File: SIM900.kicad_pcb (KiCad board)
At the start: 4 copper layers, 88 x 127 mm, 72 parts, among them J1 Conn_01x05, J11 Conn_Coaxial_Power, J12 AudioJack2_Ground, J13 AudioJack2_Ground, J2 Conn_01x04, J3 Conn_01x04, J4 Conn_01x06, J5 Conn_01x02, J6 Conn_01x06, J7 Conn_01x03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

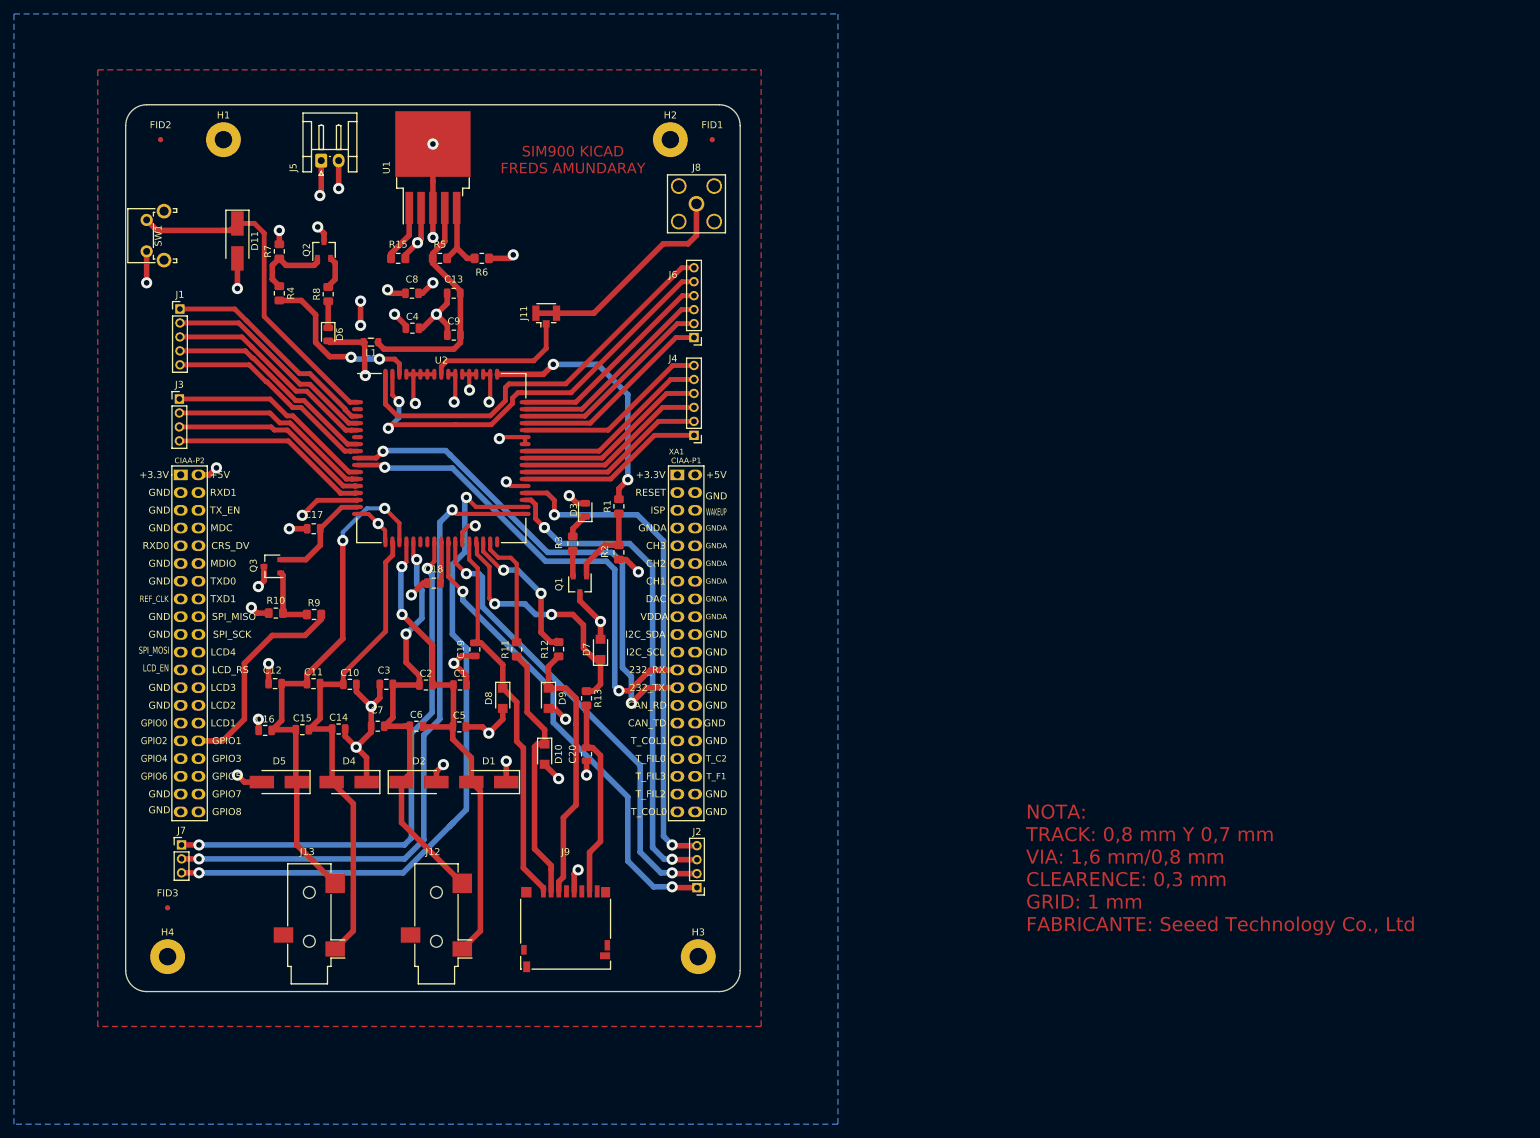
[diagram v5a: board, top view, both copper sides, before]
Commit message: Correccion de los comentarios realizados por el profesor al PCB
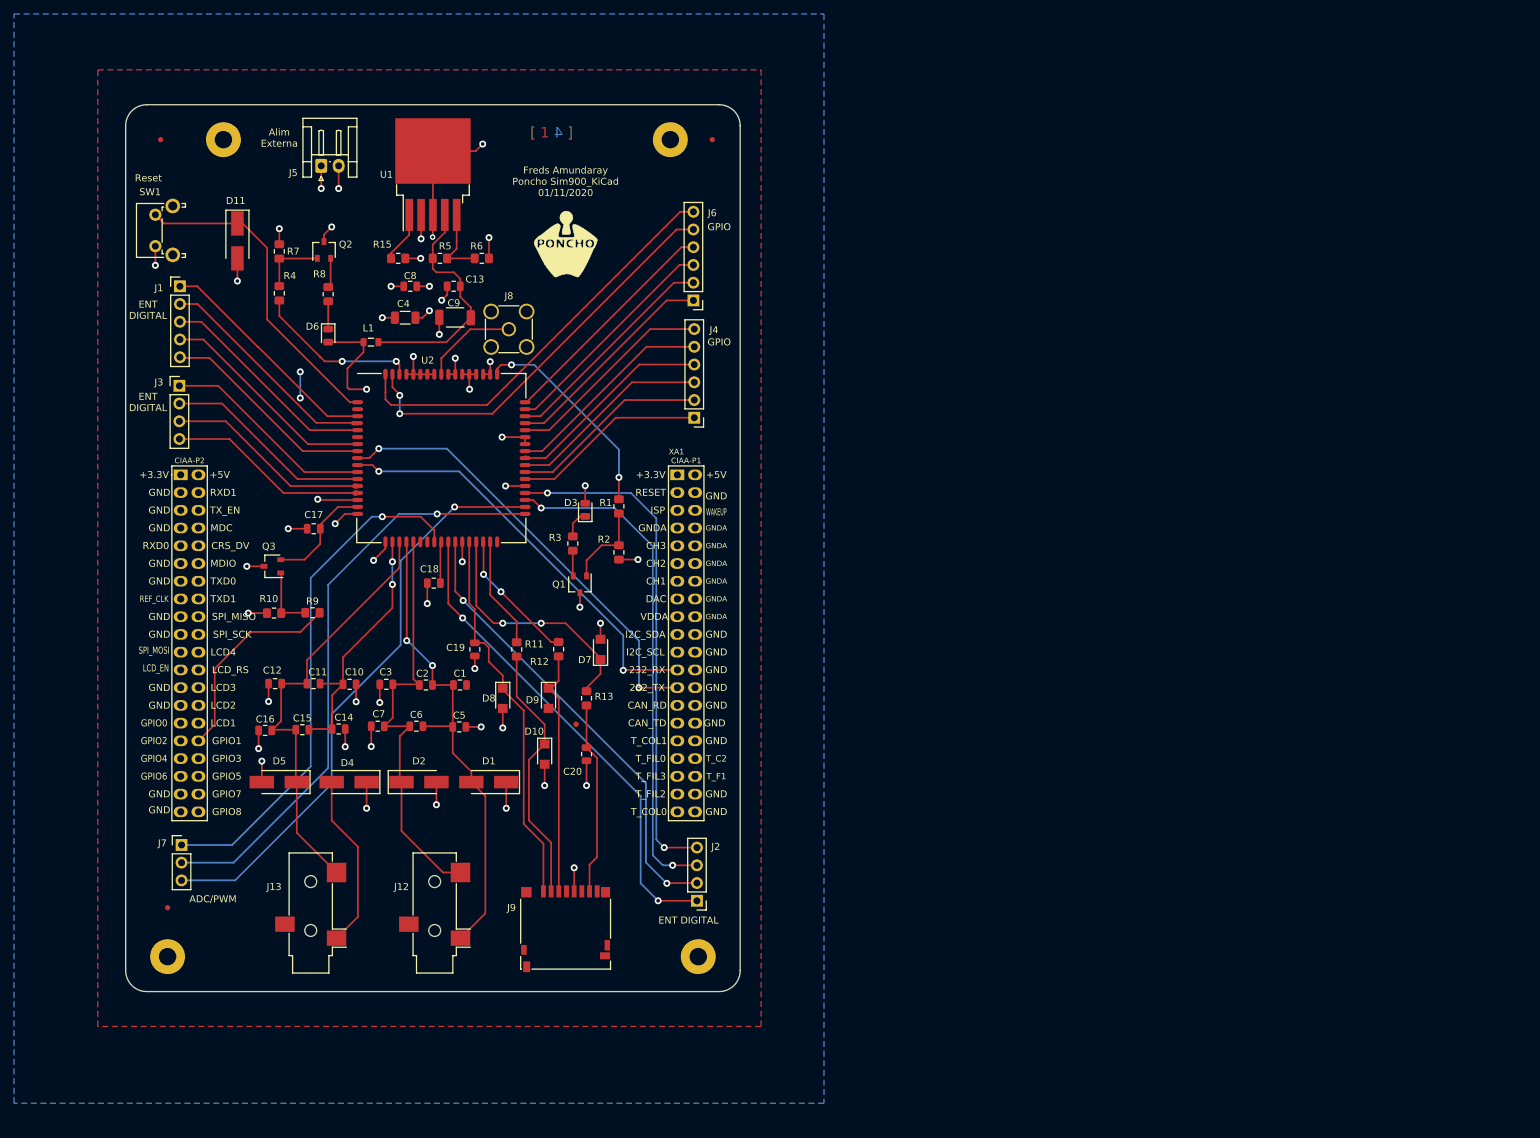
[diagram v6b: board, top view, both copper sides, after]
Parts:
- removed J11: Conn_Coaxial_Power, Connector_Coaxial:U.FL_Hirose_U.FL-R-SMT-1_Vertical
- added G***: LOGO, Poncho_Esqueleto:Logo_Poncho, F.Cu at (112.0, 58.0)
- C4: footprint Capacitor_SMD:C_0805_2012Metric -> Capacitor_SMD:C_1206_3216Metric
- C9: footprint Capacitor_SMD:C_0805_2012Metric -> Footprint:C_2312_2020Metric_Pad3.2x6.0mm_HandSolder
- J1: footprint Connector_PinHeader_2.00mm:PinHeader_1x05_P2.00mm_Vertical -> Connector_PinHeader_2.54mm:PinHeader_1x05_P2.54mm_Vertical
- J2, J3: footprint Connector_PinHeader_2.00mm:PinHeader_1x04_P2.00mm_Vertical -> Connector_PinHeader_2.54mm:PinHeader_1x04_P2.54mm_Vertical
- J4, J6: footprint Connector_PinHeader_2.00mm:PinHeader_1x06_P2.00mm_Vertical -> Connector_PinHeader_2.54mm:PinHeader_1x06_P2.54mm_Vertical
- J7: footprint Connector_PinHeader_2.00mm:PinHeader_1x03_P2.00mm_Vertical -> Connector_PinHeader_2.54mm:PinHeader_1x03_P2.54mm_Vertical
- J8: footprint Connector_Coaxial:SMA_Amphenol_132203-12_Horizontal -> Connector_Coaxial:SMA_Amphenol_901-144_Vertical
- moved J8 32.3 mm to (103.9, 70.2), turned to 0 degrees
- moved J6 5.32 mm to (130.3, 66.0)
- moved J1 3.25 mm to (56.8, 64.0)
- moved J4 2.52 mm to (130.4, 82.8)
- moved C9 2.50 mm to (96.1, 68.5)
- moved J3 1.89 mm to (56.7, 78.2)
- moved J2 1.89 mm to (130.8, 152.0)
- moved C4 1.82 mm to (89.0, 68.5), turned to 180 degrees
- moved J12 1.57 mm to (93.2, 153.8)
- moved J13 1.56 mm to (75.5, 153.8)
- moved SW1 1.46 mm to (53.2, 58.2)
- moved C8 1.03 mm to (89.8, 64.0)
- moved C13 1.00 mm to (96.0, 64.0)
- moved U1 1.00 mm to (93.0, 48.0)
- moved J5 0.75 mm to (77.0, 46.8)
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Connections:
- J8 pad 1: Net-(J11-Pad2) -> Net-(J8-Pad1)
- U2 pad 60: Net-(J11-Pad1) -> Net-(J8-Pad1)
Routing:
- net GND: track 173.2 -> 140.6 mm, vias 36 -> 43
- net Net-(J11-Pad2): track 32.1 -> 0.00 mm
- net Net-(J11-Pad1): track 20.7 -> 0.00 mm
- net Net-(J7-Pad3): track 100.8 -> 84.3 mm, vias 2 -> 1
- net Net-(J8-Pad1): track 0.00 -> 13.7 mm
- net Net-(C11-Pad1): track 76.3 -> 63.1 mm, vias 2 -> 0
- net +5V: track 77.5 -> 64.7 mm
- net Net-(J5-Pad1): track 67.4 -> 55.8 mm
- net Net-(J7-Pad2): track 95.4 -> 85.3 mm, vias 2 -> 1
- net /TXD: track 70.3 -> 60.9 mm
- net Net-(C10-Pad1): track 71.3 -> 62.5 mm, vias 0 -> 2
- net /RXD: track 73.0 -> 64.5 mm
- net /NETLIGHT: track 37.1 -> 31.1 mm
- net Net-(J7-Pad1): track 77.7 -> 73.9 mm, vias 2 -> 1
- net Net-(D9-Pad1): track 38.4 -> 35.1 mm
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- added copper zone on In2.Cu_VCD, net +3V3
- added copper zone on In1.Cu_GND, net GND
- removed copper zone on In1.Cu_VCD, net +3V3
- removed copper zone on In2.Cu_GND, net GND
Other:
- net class Default: clearance 0.3 -> 0.25
- rule trace_clearance: 0.3 -> 0.25
- board text added: "ADC/PWM"
- board text added: "Alim Externa"
- board text added: "ENT DIGITAL"
- board text added: "Freds Amundaray Poncho Sim900_KiCad 01/11/2020"
- board text added: "GPIO"
- board text added: "Nota: Minimos (MAYER 10 mils) Track: 0,25 mm Via: 1,0/ 0,5 mm Clearence: 0,25 mm distance to edge: 0,3 mm Grid: 1 mm / 0,5 mm / 0,25 mm Terminacion: HASL sin plomo"
- board text added: "Reset"
- board text added: "[ 1 ]"
- board text added: "[ 2 ]"
- board text added: "[ 3 ]"
- board text added: "[ 4 ]"
- board text removed: "NOTA: TRACK: 0,8 mm Y 0,7 mm VIA: 1,6 mm/0,8 mm CLEARENCE: 0,3 mm GRID: 1 mm FABRICANTE: Seeed Technology Co., Ltd"
- board text removed: "SIM900 KICAD FREDS AMUNDARAY"

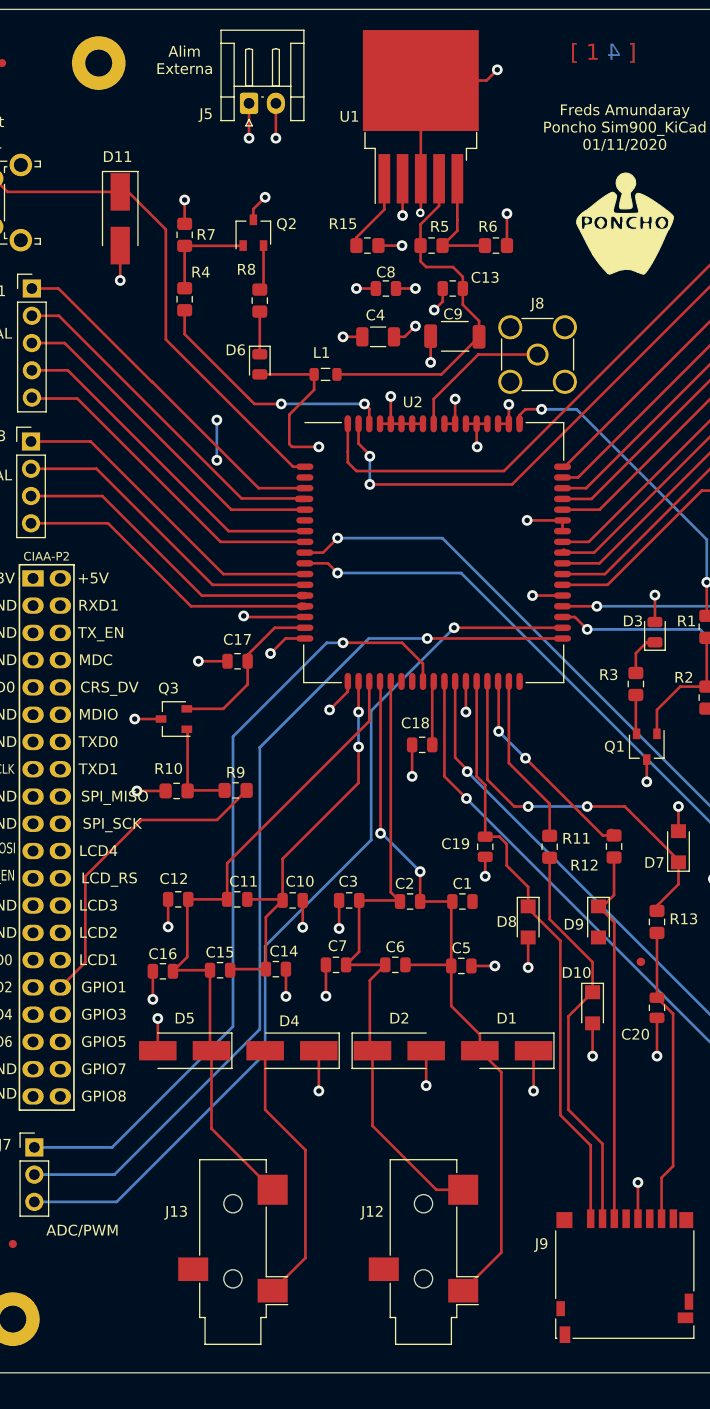
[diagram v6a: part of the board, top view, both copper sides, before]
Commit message: se corrigio algunas cosas faltantes de las observaciones realizadas
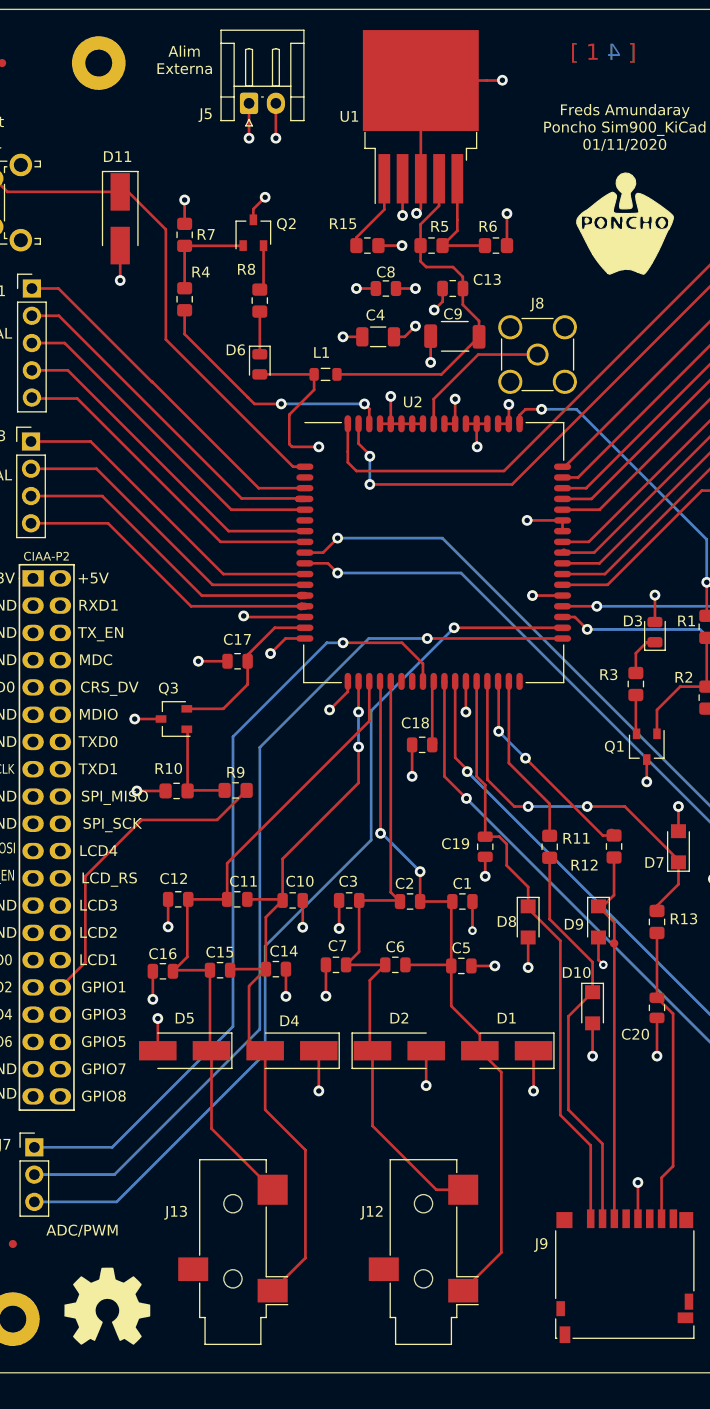
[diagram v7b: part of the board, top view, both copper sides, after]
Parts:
- added G101: Logo_OSHWA, Poncho_Esqueleto:Logo_OSHWA, F.Cu at (63.8, 158.8)
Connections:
- XA1 pad 2: Net-(XA1-Pad2) -> +5V
- XA1 pad 42: +5V -> Net-(XA1-Pad42)
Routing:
- net Net-(C10-Pad1): track 62.5 -> 72.0 mm
- net +5V: track 64.7 -> 72.7 mm
- net GND: track 140.6 -> 146.0 mm, vias 43 -> 45
- net Net-(J5-Pad1): vias 4 -> 2
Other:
- board text added: "Nota: Minimos (MAYER 10 mils) Track: 0,25 mm Via: 1,0/ 0,5 mm Clearence: 0,25 mm distance to edge: 0,3 mm Grid: 1 mm / 0,5 mm / 0,25 mm / 0,20 mm Terminacion: HASL sin plomo Licenciado en: CERN Open Hardware version 2 - permisive"
- board text removed: "Nota: Minimos (MAYER 10 mils) Track: 0,25 mm Via: 1,0/ 0,5 mm Clearence: 0,25 mm distance to edge: 0,3 mm Grid: 1 mm / 0,5 mm / 0,25 mm Terminacion: HASL sin plomo"
